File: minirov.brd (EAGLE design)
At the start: 65.8 x 51.6 mm, 66 parts, among them Q1 DMN6140L-13DICT-ND, Q2 DMN6140L-13DICT-ND, U1 DRV8848PWP, U2 DRV8848PWP, U4 S811-1X1T-06-F, Y1 ABM8-25.000MHZ-B2-T

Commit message: routing
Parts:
- moved C8 20.8 mm to (4.95, -14.2), turned to 145 degrees
- moved C6 17.5 mm to (18.8, -17.3), turned to 270 degrees
- moved C7 16.3 mm to (4.93, -9.93), turned to 45 degrees
- moved Y1 15.9 mm to (6.93, -11.9), turned to 319 degrees
- moved C9 13.3 mm to (4.11, -8.31), turned to 45 degrees
- moved C2 13.3 mm to (14.7, -15.0), flipped to the bottom, turned to 180 degrees
- moved D1 8.85 mm to (3.91, -18.1)
- moved R10 8.79 mm to (7.67, -18.0)
- moved U3 7.43 mm to (15.2, -10.8), turned to 90 degrees
- moved C3 6.37 mm to (14.7, -10.3), flipped to the bottom, turned to 180 degrees
- moved R2 5.54 mm to (16.0, -3.05), flipped to the bottom, turned to 90 degrees
- moved R11 5.52 mm to (7.67, -16.4)
- moved D3 5.50 mm to (4.04, -16.4)
- moved R3 5.11 mm to (19.9, -4.42), flipped to the bottom, turned to 90 degrees
- moved C4 4.40 mm to (14.7, -8.64), flipped to the bottom, turned to 180 degrees
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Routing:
- net +3V3: track 124.4 -> 200.7 mm, vias 5 -> 12
- net CS: track 0.00 -> 57.1 mm, vias 0 -> 5
- net INT: track 0.00 -> 49.7 mm, vias 0 -> 3
- net SCK: track 0.00 -> 46.6 mm, vias 0 -> 3
- net MISO: track 0.00 -> 44.9 mm, vias 0 -> 3
- net MOSI: track 0.00 -> 42.8 mm, vias 0 -> 3
- net TPOUT+: track 0.00 -> 24.9 mm
- net TPOUT-: track 0.00 -> 22.5 mm, vias 0 -> 2
- net TPIN-: track 0.00 -> 18.7 mm, vias 0 -> 2
- net TPIN+: track 0.00 -> 18.0 mm, vias 0 -> 2
- net N$29: track 0.00 -> 16.7 mm
- net N$1: track 0.00 -> 7.02 mm
- net N$2: track 0.00 -> 6.95 mm
- net RST: track 0.00 -> 6.29 mm, vias 0 -> 1
- net LEDA: track 0.00 -> 5.76 mm
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
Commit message: couple checks and fixes
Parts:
- moved C2 0.36 mm to (15.0, -15.0)
- turned C7 to 49 degrees
- turned C8 to 139 degrees
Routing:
- net GND: track 47.5 -> 71.5 mm, vias 4 -> 30
- net N$4: track 0.00 -> 2.05 mm
- net N$5: track 0.00 -> 1.91 mm
- net N$9: track 0.00 -> 1.81 mm
- net N$3: track 0.00 -> 1.59 mm

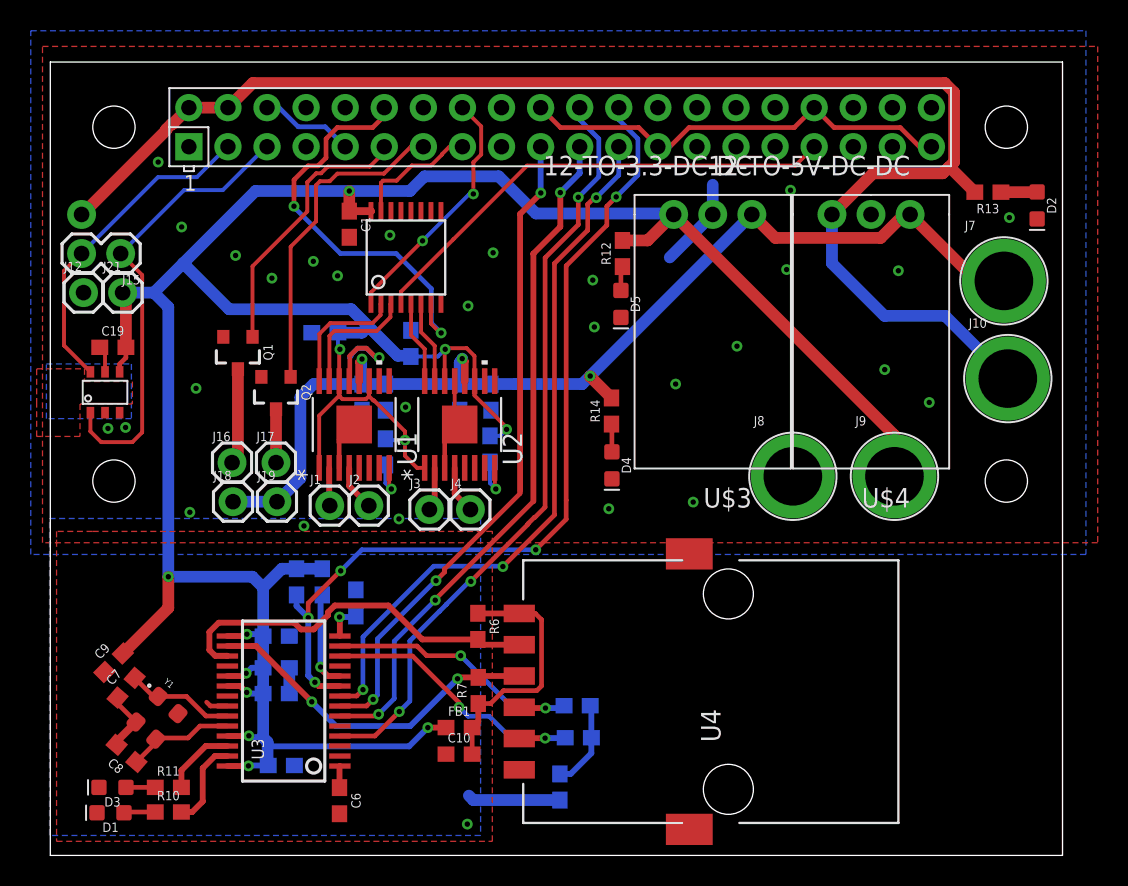
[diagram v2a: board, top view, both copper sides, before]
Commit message: labels and ground stitching
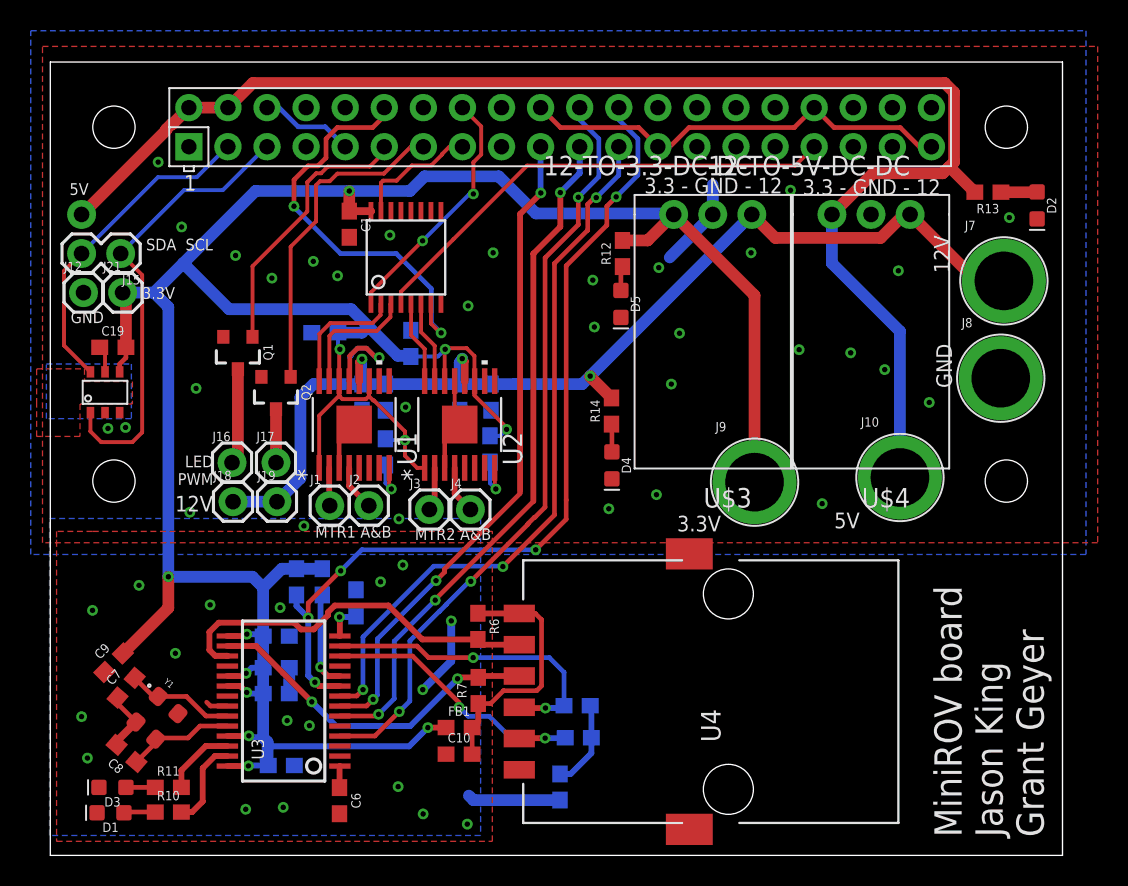
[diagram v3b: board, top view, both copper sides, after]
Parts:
- moved J8 14.9 mm to (61.8, 10.2)
- moved J10 9.51 mm to (55.2, 3.73)
- moved J9 9.10 mm to (45.8, 3.43)
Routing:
- net GND: track 71.5 -> 76.8 mm, vias 30 -> 51
- net +3V3: track 200.8 -> 197.4 mm
- net TPIN+: track 18.0 -> 20.4 mm
- net +5V: track 94.5 -> 95.7 mm
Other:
- board text added: "12V"
- board text added: "3.3 - GND - 12"
- board text added: "3.3V"
- board text added: "5V"
- board text added: "GND"
- board text added: "LED PWM"
- board text added: "MTR1 A&B"
- board text added: "MTR2 A&B"
- board text added: "MiniROV board Jason King Grant Geyer"
- board text added: "SDA SCL"

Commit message: fixed airwire
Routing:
- net +3V3: track 197.4 -> 199.7 mm, vias 12 -> 13
- net GND: vias 51 -> 57
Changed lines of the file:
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@@
 <via x="23.0886" y="8.3058" extent="1-16" drill="0.35"/>
 <via x="22.6568" y="1.0414" extent="1-16" drill="0.35"/>
-<via x="16.4846" y="0.5842" extent="1-16" drill="0.35"/>
+<via x="17.5768" y="-0.1778" extent="1-16" drill="0.35"/>
 <via x="36.2966" y="1.7018" extent="1-16" drill="0.35"/>
 <via x="50.165" y="2.032" extent="1-16" drill="0.35"/>
@@
 <wire x1="26.0604" y1="-8.2042" x2="26.0604" y2="-5.588" width="0.508" layer="16"/>
 <via x="14.9352" y="-4.7244" extent="1-16" drill="0.35"/>
-<wire x1="19.7485" y1="7.1755" x2="20.2565" y2="8.1035" width="0" layer="19" extent="1-16"/>
+<via x="17.7546" y="7.874" extent="1-16" drill="0.35"/>
+<via x="14.097" y="-0.2032" extent="1-16" drill="0.35"/>
+<via x="14.5288" y="12.3952" extent="1-16" drill="0.35"/>
+<via x="16.6116" y="11.4046" extent="1-16" drill="0.35"/>
+<via x="17.8054" y="6.604" extent="1-16" drill="0.35"/>
+<via x="34.6456" y="7.5438" extent="1-16" drill="0.35"/>
 </signal>
 <signal name="+3V3">
@@
 <wire x1="23.0505" y1="5.1435" x2="23.0505" y2="6.1595" width="0.254" layer="1"/>
 <wire x1="23.8379" y1="4.3561" x2="23.0505" y2="5.1435" width="0.254" layer="1"/>
-<wire x1="17.473459375" y1="7.752434375" x2="18.78849375" y2="9.06746875" width="0.254" layer="1"/>
-<wire x1="17.473459375" y1="4.3561" x2="17.473459375" y2="7.752434375" width="0.254" layer="1"/>
 <wire x1="18.78849375" y1="9.019925" x2="18.78849375" y2="9.06746875" width="0.254" layer="1"/>
 <wire x1="22.5815" y1="11.645" x2="23.3825" y2="11.645" width="0.762" layer="16"/>
@@
 <wire x1="14.4018" y1="-13.7414" x2="14.1224" y2="-13.462" width="0.381" layer="16"/>
 <wire x1="13.8058" y1="-13.1454" x2="13.8312" y2="-13.1708" width="0.762" layer="16"/>
+<wire x1="17.473459375" y1="4.3561" x2="17.473459375" y2="3.068484375" width="0.3048" layer="1"/>
+<via x="15.0486" y="-2.198" extent="1-16" drill="0.35"/>
+<wire x1="15.0486" y1="0.643625" x2="15.0486" y2="-2.198" width="0.3048" layer="1"/>
+<wire x1="17.473459375" y1="3.068484375" x2="15.0486" y2="0.643625" width="0.3048" layer="1"/>
 </signal>
 <signal name="MTR_1A_PWM">

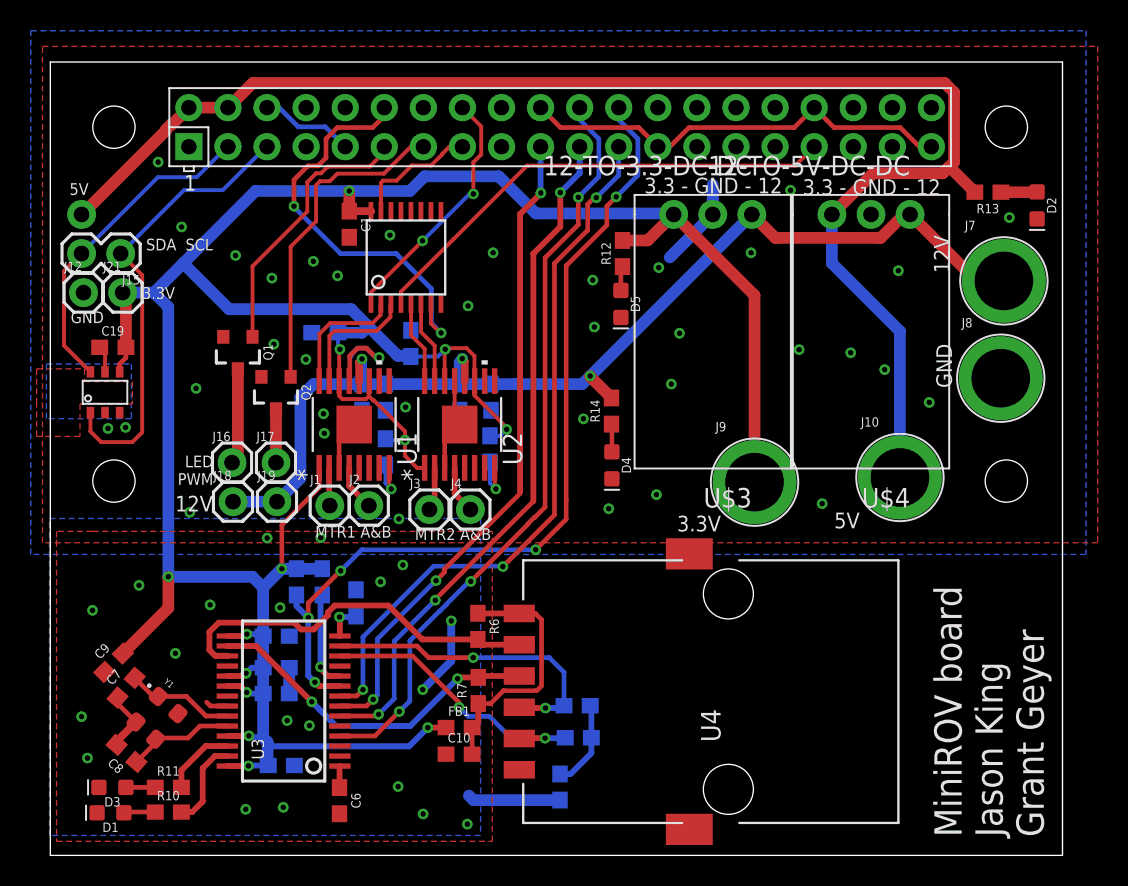
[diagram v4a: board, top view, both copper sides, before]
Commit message: last airwire and a DRC check
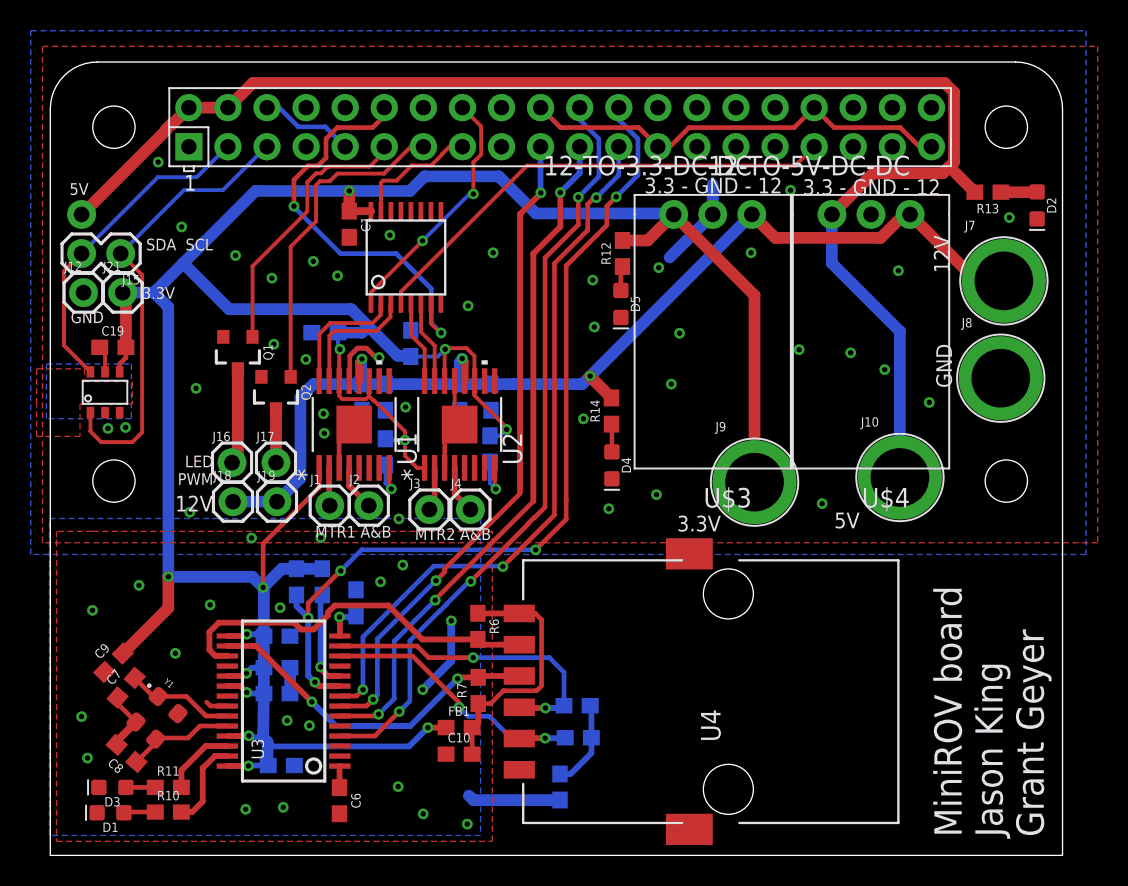
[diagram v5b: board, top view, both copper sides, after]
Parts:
- moved C3 0.05 mm to (14.7, -10.3)
- moved C4 0.05 mm to (14.7, -8.64)
- moved C5 0.05 mm to (14.7, -6.58)
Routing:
- net +3V3: track 199.7 -> 201.6 mm
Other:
- outline, holes or cut-outs redrawn
